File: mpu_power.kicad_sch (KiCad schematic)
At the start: 50 parts, among them U401 STM32MP135FAE7

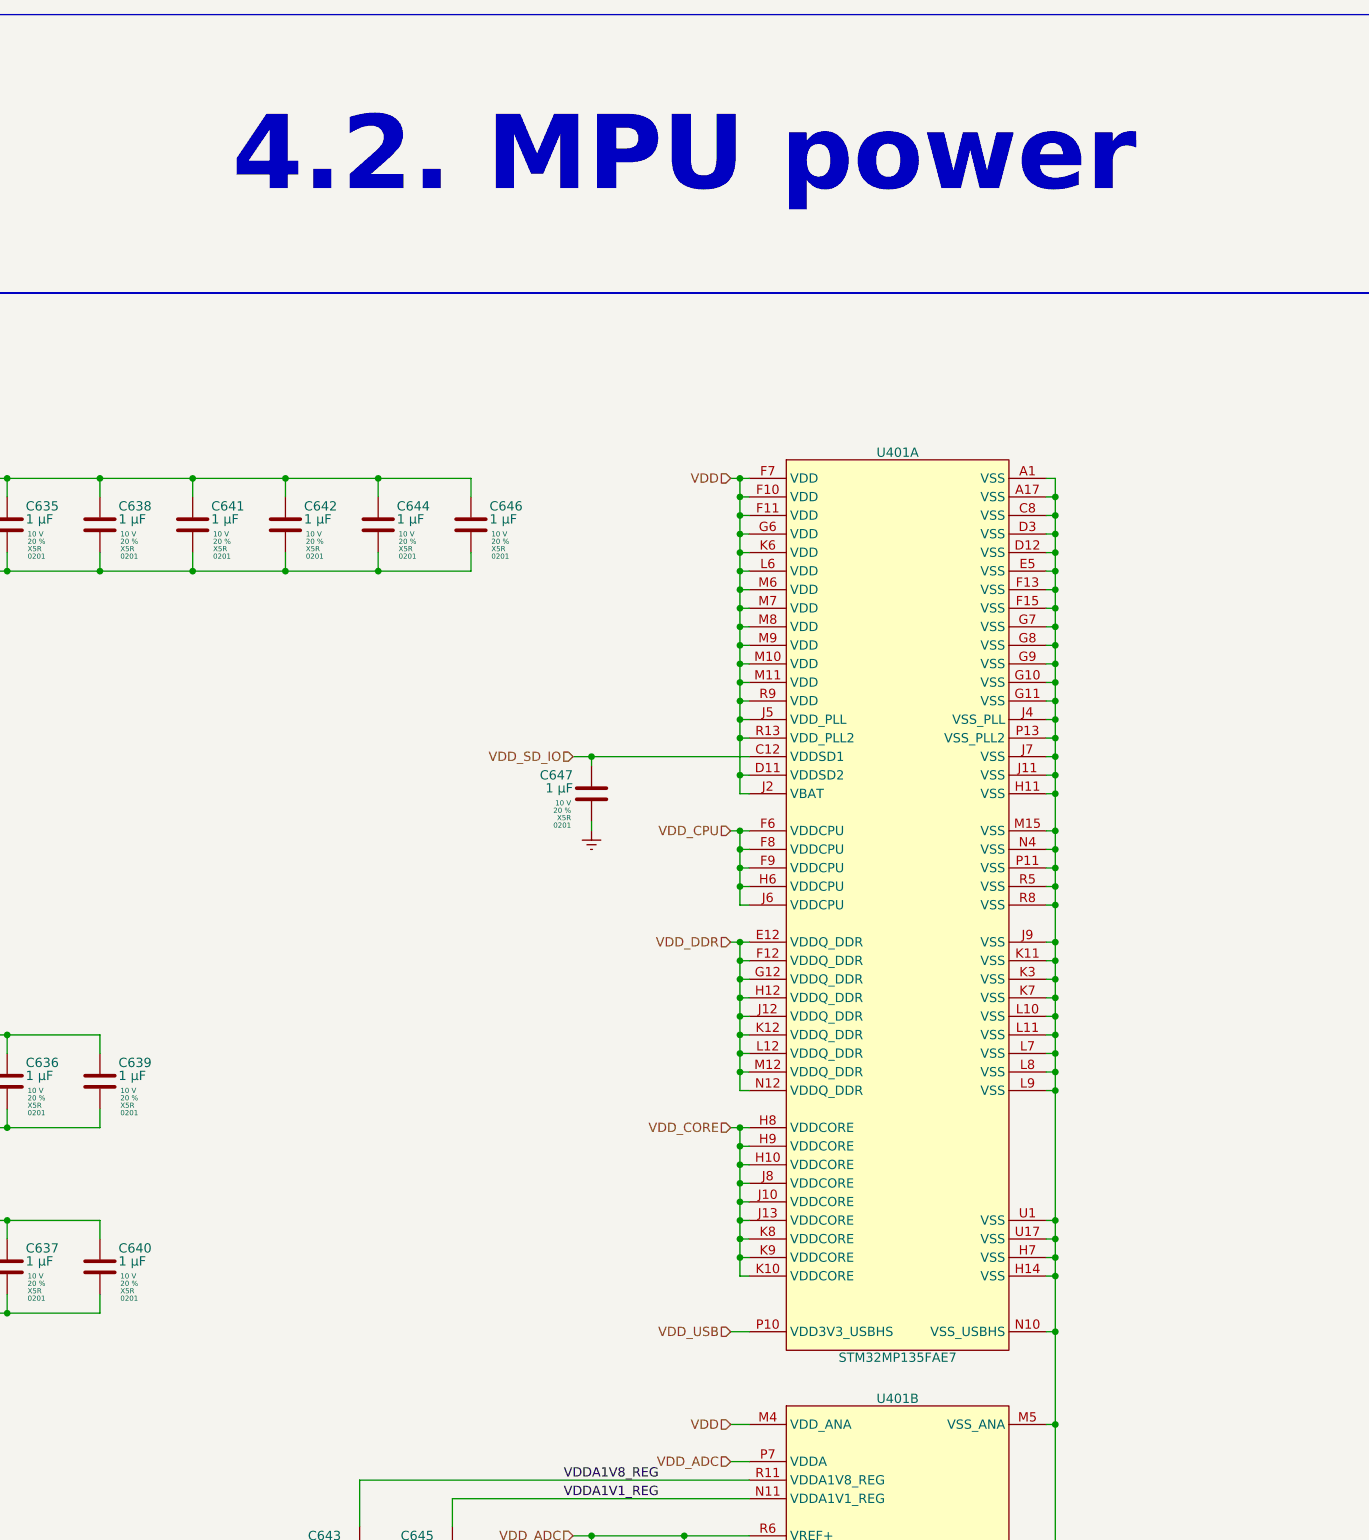
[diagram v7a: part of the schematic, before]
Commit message: Rework the schematics
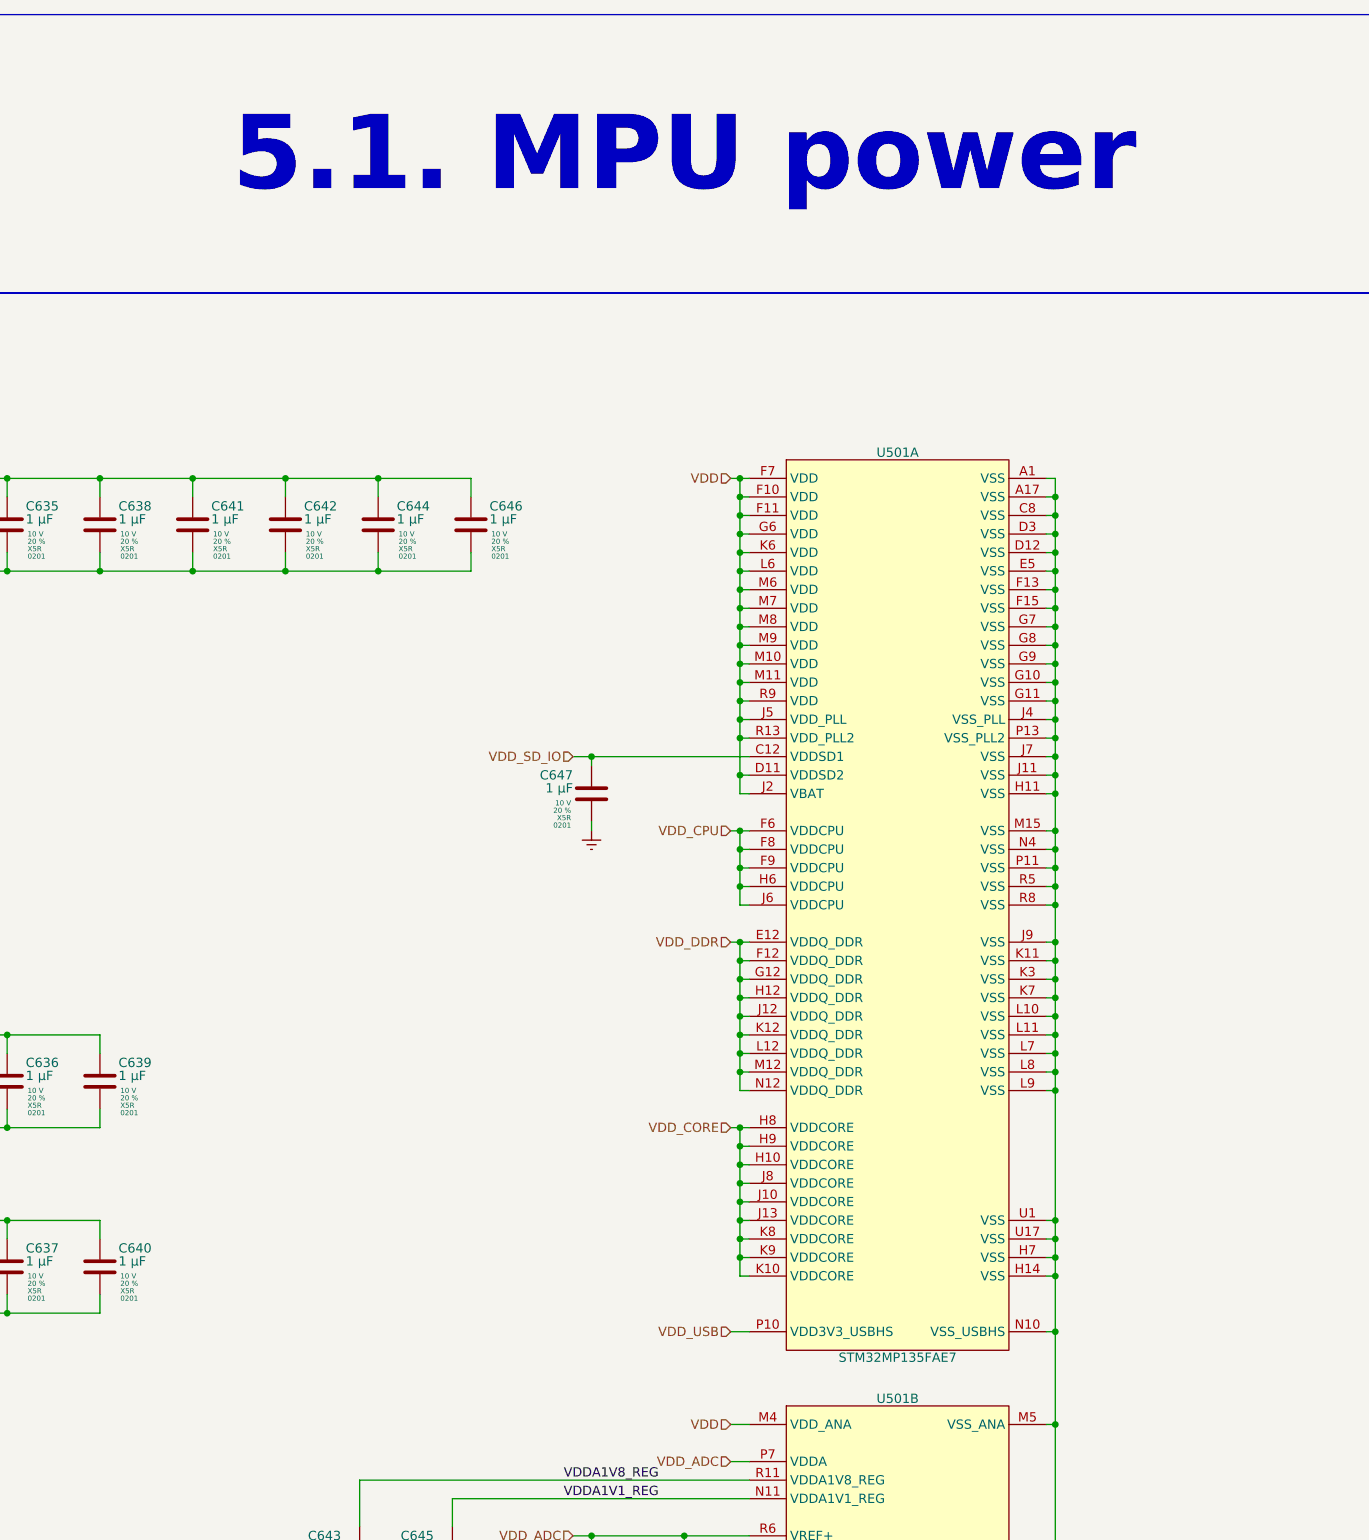
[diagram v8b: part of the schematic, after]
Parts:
- renumbered U401 to U501
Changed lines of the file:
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@@
 	(title_block
 		(title "Linux SBC")
-		(date "2025-12-17")
+		(date "2025-12-19")
 		(rev "v1.0.0")
 	)
@@
 		)
 	)
-	(text_box "4.2. MPU power"
+	(text_box "5.1. MPU power"
 		(exclude_from_sim no)
 		(at 12.7 12.7 0)
@@
 		(on_board yes)
 		(dnp no)
-		(property "Reference" "U401"
+		(property "Reference" "U501"
 			(at 238.76 202.946 0)
 			(effects
@@
 			(project "linux-sbc"
 				(path "/fa11a02f-8043-4153-ab69-88d766503017/2d01087b-54dc-4f43-9cc7-a0ba17201776/38fb80ce-3aa2-4a17-bb8b-7759011755a2"
-					(reference "U401")
+					(reference "U501")
 					(unit 2)
 				)
@@
 		(on_board yes)
 		(dnp no)
-		(property "Reference" "U401"
+		(property "Reference" "U501"
 			(at 238.76 73.406 0)
 			(effects
@@
 			(project "linux-sbc"
 				(path "/fa11a02f-8043-4153-ab69-88d766503017/2d01087b-54dc-4f43-9cc7-a0ba17201776/38fb80ce-3aa2-4a17-bb8b-7759011755a2"
-					(reference "U401")
+					(reference "U501")
 					(unit 1)
 				)
